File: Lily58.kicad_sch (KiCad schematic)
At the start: 0 parts

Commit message: brainstorming with some components in the schematic
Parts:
- added BAT: Conn_01x02_Pin, Connector_JST:JST_EH_B2B-EH-A_1x02_P2.50mm_Vertical, symbol Connector:Conn_01x02_Pin
- added J1: USB_C_Receptacle, Connector_USB:USB_C_Receptacle_Amphenol_12401548E4-2A_CircularHoles, symbol Connector:USB_C_Receptacle
- added U1: ESP32-S3-WROOM-2, PCM_Espressif:ESP32-S3-WROOM-2, symbol PCM_Espressif:ESP32-S3-WROOM-2
- added U2: D3V3XA4B10LP, Package_DFN_QFN:Diodes_UDFN-10_1.0x2.5mm_P0.5mm, symbol Power_Protection:D3V3XA4B10LP
- added U3: BQ24090DGQ, Package_SO:HVSSOP-10-1EP_3x3mm_P0.5mm_EP1.57x1.88mm_ThermalVias, symbol Battery_Management:BQ24090DGQ
- added U4: AP63203WU, Package_TO_SOT_SMD:TSOT-23-6, symbol Regulator_Switching:AP63203WU
- added Y1: Crystal_GND24, Crystal:Crystal_SMD_3225-4Pin_3.2x2.5mm_HandSoldering, symbol Device:Crystal_GND24
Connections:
- new net: U2.3 (VSS), U2.8 (VSS)
- new net: U3.11 (VSS), U3.3 (VSS)
- new net: J1.A1 (GND), J1.A12 (GND), J1.B1 (GND), J1.B12 (GND)
- new net: J1.A4 (VBUS), J1.A9 (VBUS), J1.B4 (VBUS), J1.B9 (VBUS)
- new net NO: U1.1 (GND), U1.13 (GPIO19/U1RTS/ADC2_CH8/CLK_OUT2/USB_D-), U1.14 (GPIO20/U1CTS/ADC2_CH9/CLK_OUT1/USB_D+), U1.2 (3V3), U1.27 (GPIO0/BOOT), U1.36 (U0RXD/GPIO44/CLK_OUT2), U1.37 (U0TXD/GPIO43/CLK_OUT1), U1.40 (GND), U1.41 (GND)

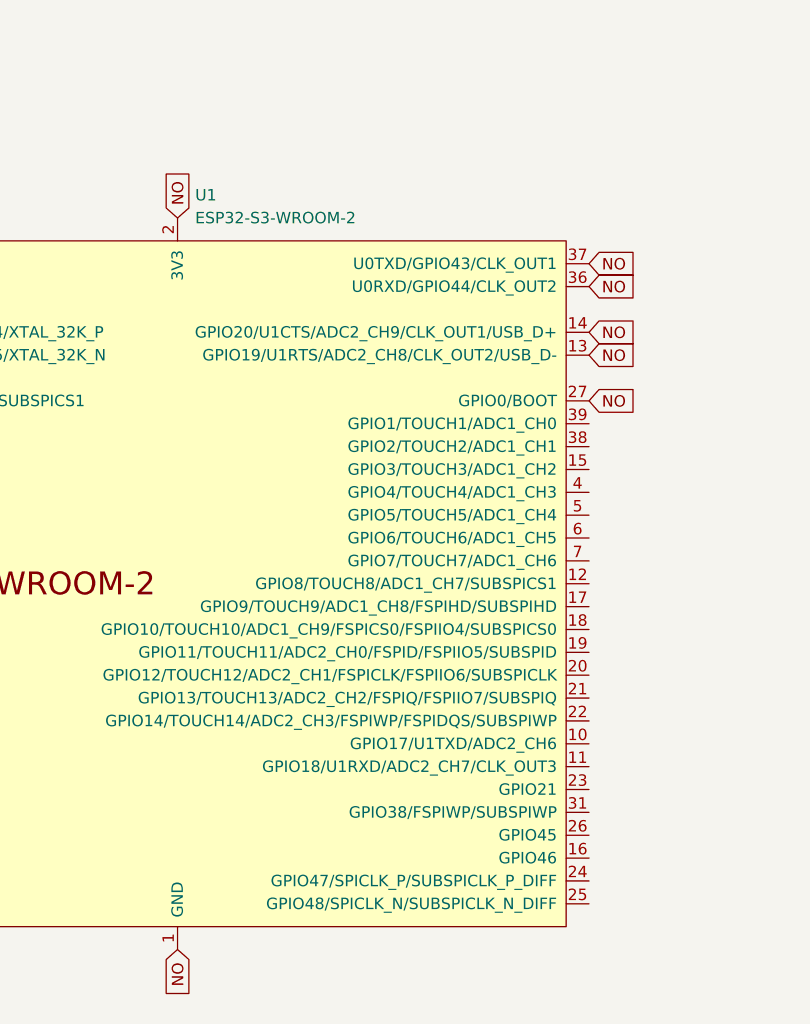
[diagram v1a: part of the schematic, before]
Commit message: added datasheets for MCU, bat-charger & voltage regulator
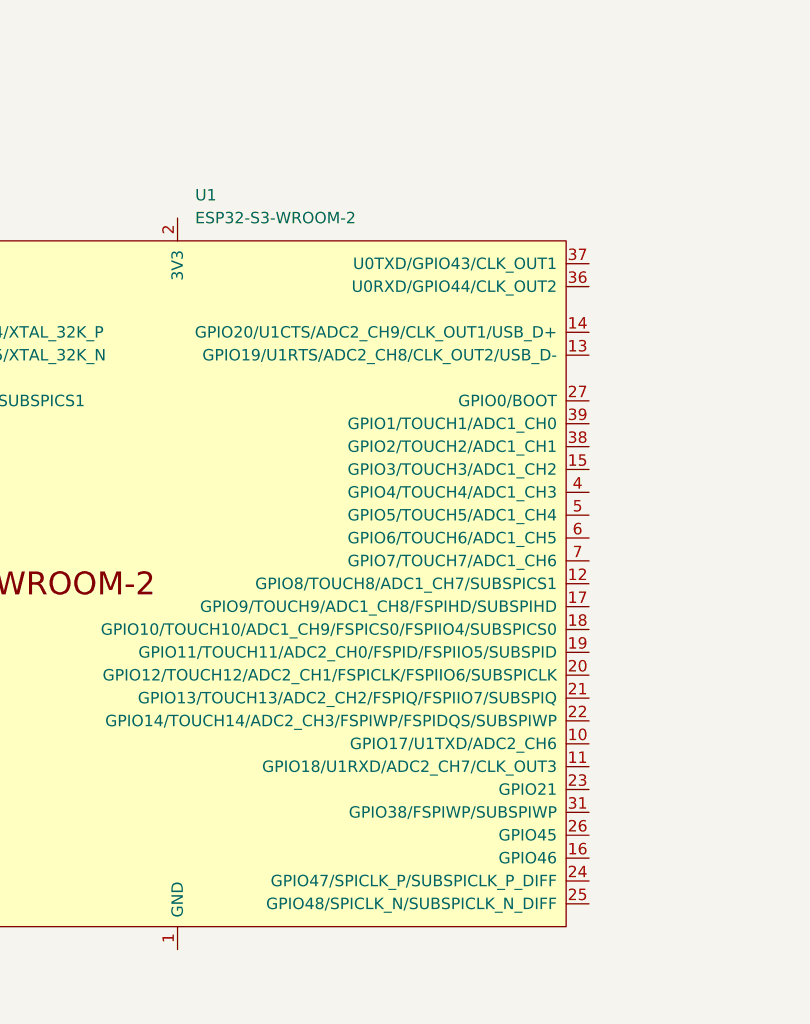
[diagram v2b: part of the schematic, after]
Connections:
- removed net NO: U1.1 (GND), U1.13 (GPIO19/U1RTS/ADC2_CH8/CLK_OUT2/USB_D-), U1.14 (GPIO20/U1CTS/ADC2_CH9/CLK_OUT1/USB_D+), U1.2 (3V3), U1.27 (GPIO0/BOOT), U1.36 (U0RXD/GPIO44/CLK_OUT2), U1.37 (U0TXD/GPIO43/CLK_OUT1), U1.40 (GND), U1.41 (GND)
- new net: U1.1 (GND), U1.40 (GND), U1.41 (GND)
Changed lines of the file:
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@@
 (kicad_sch (version 20230121) (generator eeschema)
   (paper "A4")
-  (global_label "NO" (shape input) (at 138.43 114.3 0) (fields_autoplaced)
-    (effects (font (size 1.27 1.27)) (justify left))
-    (property "Intersheetrefs" "${INTERSHEET_REFS}" (at 143.9968 114.3 0)
-      (effects (font (size 1.27 1.27)) (justify left) hide)
-    )
-  )
-  (global_label "NO" (shape input) (at 138.43 124.46 0) (fields_autoplaced)
-    (effects (font (size 1.27 1.27)) (justify left))
-    (property "Intersheetrefs" "${INTERSHEET_REFS}" (at 143.9968 124.46 0)
-      (effects (font (size 1.27 1.27)) (justify left) hide)
-    )
-  )
-  (global_label "NO" (shape input) (at 138.43 116.84 0) (fields_autoplaced)
-    (effects (font (size 1.27 1.27)) (justify left))
-    (property "Intersheetrefs" "${INTERSHEET_REFS}" (at 143.9968 116.84 0)
-      (effects (font (size 1.27 1.27)) (justify left) hide)
-    )
-  )
-  (global_label "NO" (shape input) (at 92.71 109.22 90) (fields_autoplaced)
-    (effects (font (size 1.27 1.27)) (justify left))
-    (property "Intersheetrefs" "${INTERSHEET_REFS}" (at 92.71 103.6532 90)
-      (effects (font (size 1.27 1.27)) (justify left) hide)
-    )
-  )
-  (global_label "NO" (shape input) (at 138.43 121.92 0) (fields_autoplaced)
-    (effects (font (size 1.27 1.27)) (justify left))
-    (property "Intersheetrefs" "${INTERSHEET_REFS}" (at 143.9968 121.92 0)
-      (effects (font (size 1.27 1.27)) (justify left) hide)
-    )
-  )
-  (global_label "NO" (shape input) (at 92.71 190.5 270) (fields_autoplaced)
-    (effects (font (size 1.27 1.27)) (justify right))
-    (property "Intersheetrefs" "${INTERSHEET_REFS}" (at 92.71 196.0668 90)
-      (effects (font (size 1.27 1.27)) (justify right) hide)
-    )
-  )
-  (global_label "NO" (shape input) (at 138.43 129.54 0) (fields_autoplaced)
-    (effects (font (size 1.27 1.27)) (justify left))
-    (property "Intersheetrefs" "${INTERSHEET_REFS}" (at 143.9968 129.54 0)
-      (effects (font (size 1.27 1.27)) (justify left) hide)
-    )
-  )
   (symbol (lib_id "Connector:Conn_01x02_Pin") (at 208.28 64.77 180) (unit 1)
     (in_bom yes) (on_board yes) (dnp no) (fields_autoplaced)

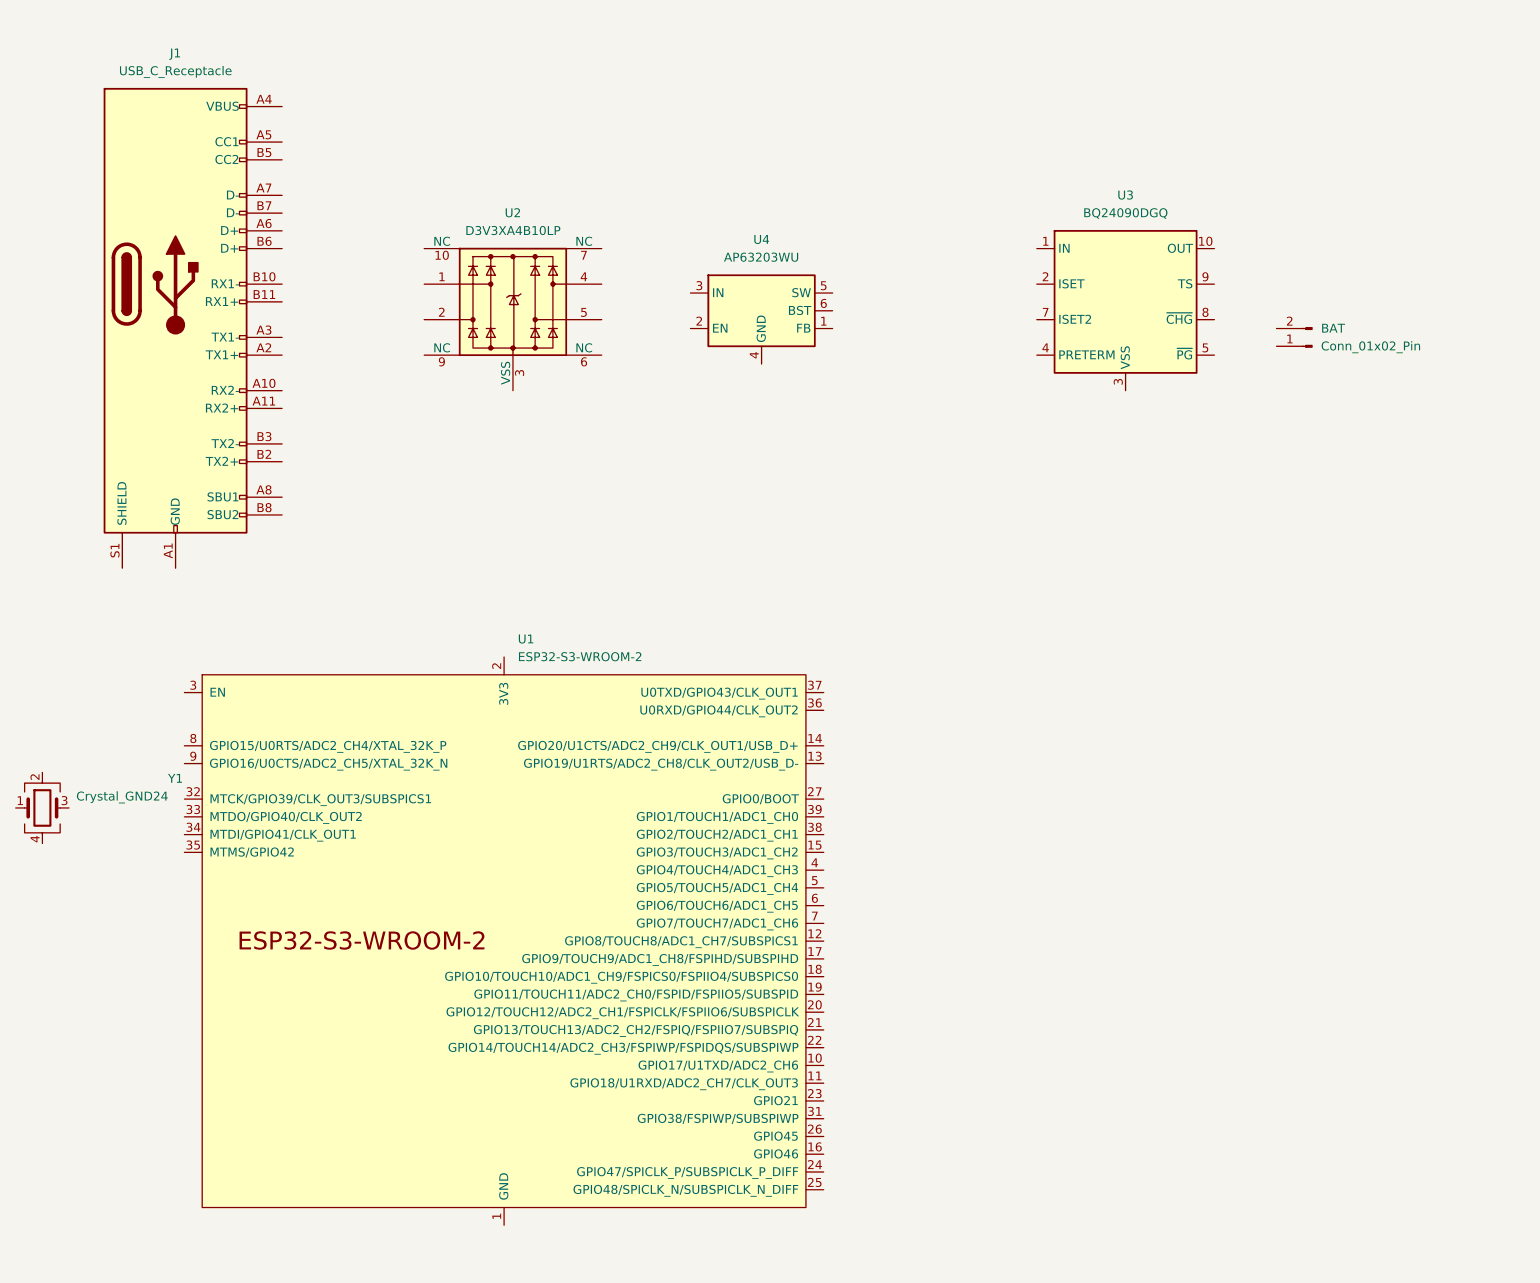
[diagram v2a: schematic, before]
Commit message: AP63203 DC/DC conv. circuit finished
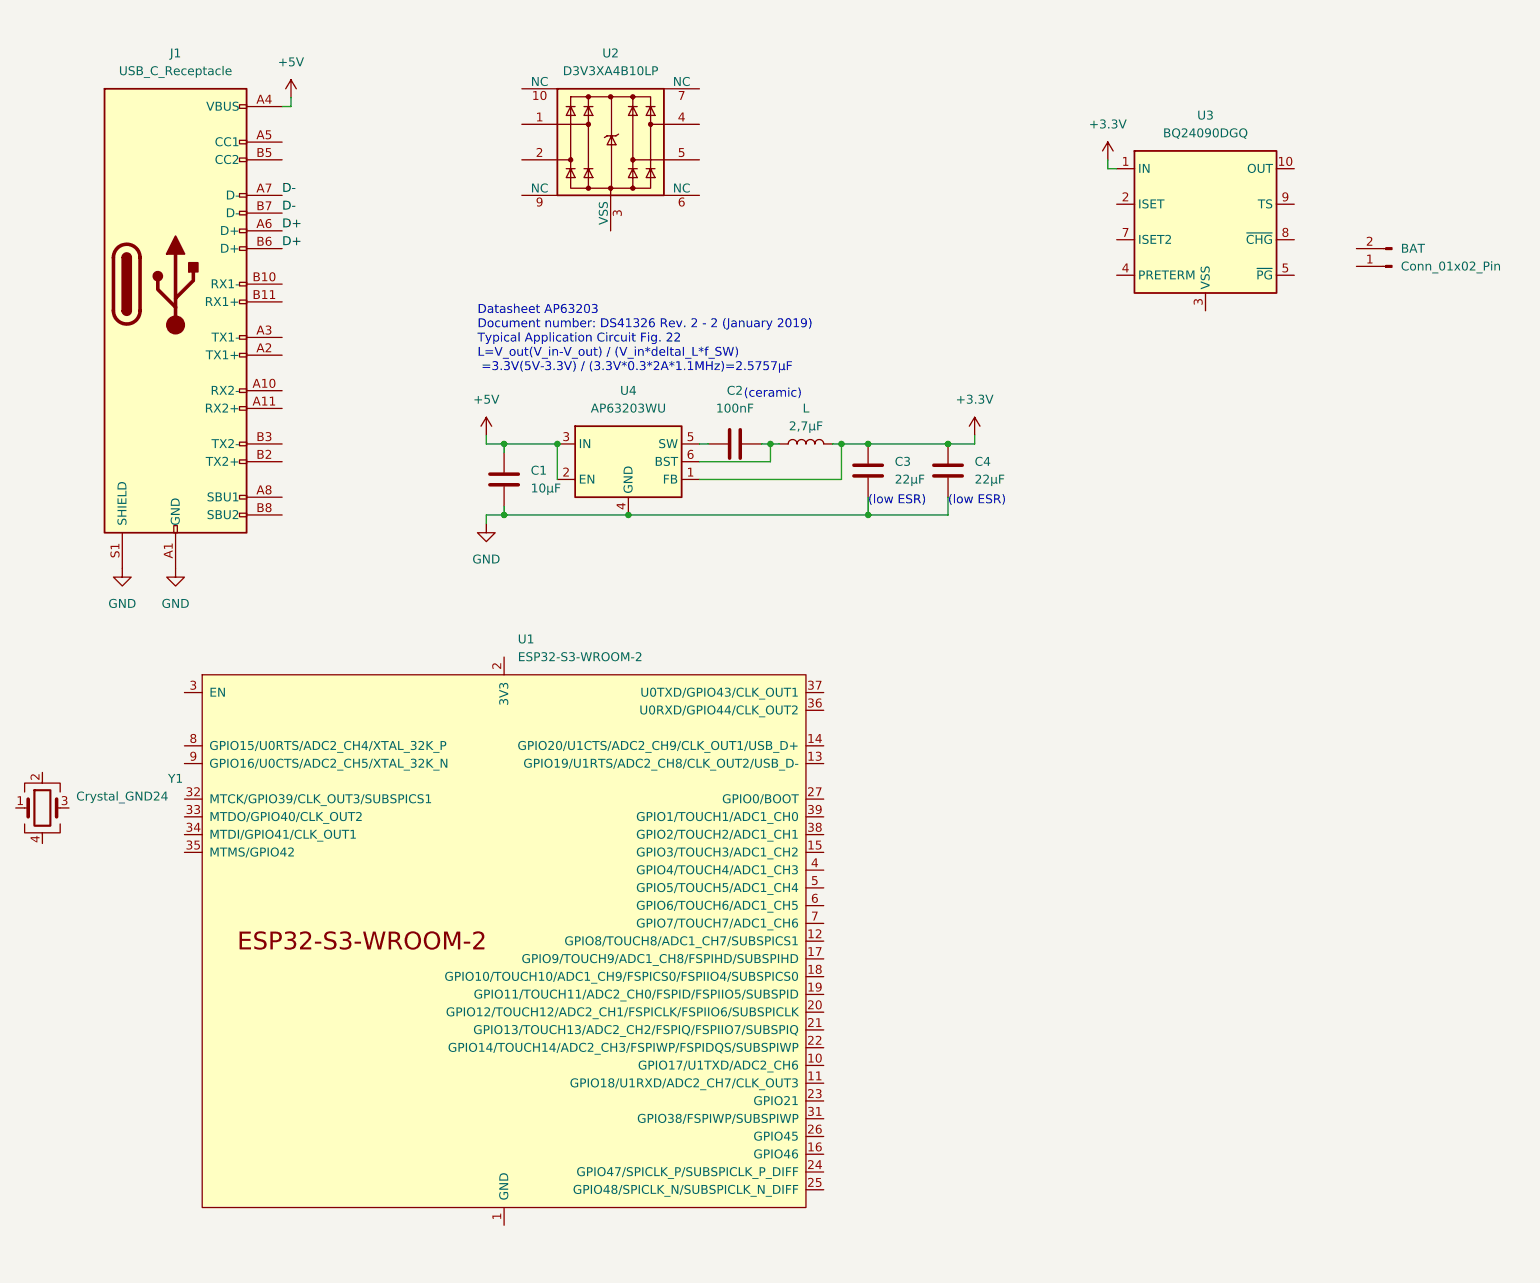
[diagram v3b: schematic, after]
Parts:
- added C1: 10µF, symbol Device:C
- added C2: 100nF, symbol Device:C
- added C3, C4: 22µF, symbol Device:C
- added L: 2,7µF, symbol Device:L
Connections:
- net +3.3V: now reaches U4.1 (FB)
- net +3.3V: now also U3.1 (IN), C3.1, C4.1, L.2
- net +5V: now reaches U4.2 (EN)
- net +5V: now also J1.A4 (VBUS), J1.A9 (VBUS), J1.B4 (VBUS), J1.B9 (VBUS), U4.3 (IN), C1.1
- net GND: now reaches U4.4 (GND)
- net GND: now also J1.A1 (GND), J1.A12 (GND), J1.B1 (GND), J1.B12 (GND), J1.S1 (SHIELD), C1.2, C3.2, C4.2
- net at U4.5 (SW): now also C2.1
- net at U4.6 (BST): now also C2.2, L.1
- net D+: now reaches J1.A6 (D+)
- net D+: now also J1.B6 (D+)
- net D-: now reaches J1.A7 (D-)
- net D-: now also J1.B7 (D-)
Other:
- note added: "(ceramic)"
- note added: "(low ESR)"
- note added: "Datasheet AP63203 Document number: DS41326 Rev. 2 - 2 (January 2019) Typical Application Circuit Fig. 22 L=V_out(V_in-V_out) / (V_in*deltaI_L*f_SW) =3.3V(5V-3.3V) / (3.3V*0.3*2A*1.1MHz)=2.5757µF"
- moved on the sheet: BAT, U2, U3, U4

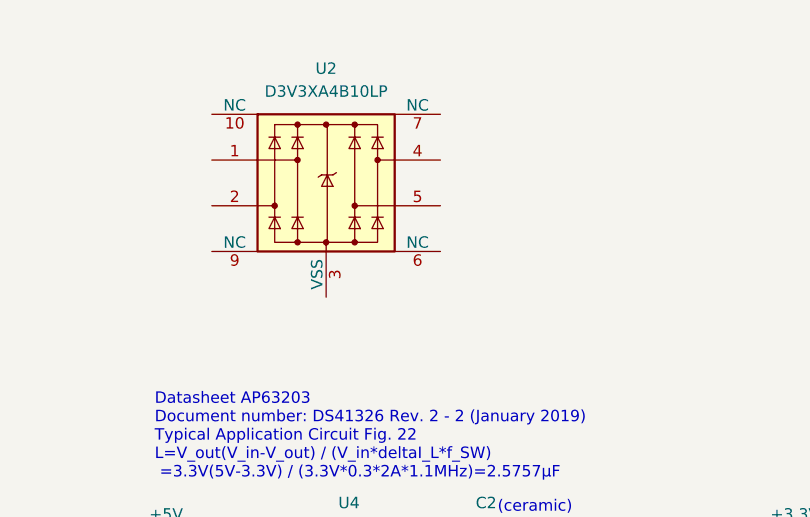
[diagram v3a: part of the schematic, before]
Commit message: TVS Diode array connected
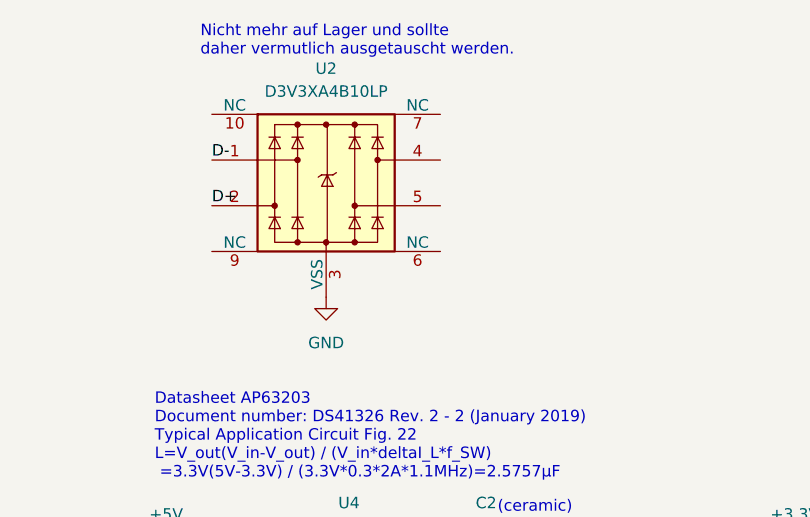
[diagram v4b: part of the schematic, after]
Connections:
- net D+: now also U2.2
- net D-: now also U2.1
- net GND: now also U2.3 (VSS), U2.8 (VSS)
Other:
- note added: "Nicht mehr auf Lager und sollte daher vermutlich ausgetauscht werden."
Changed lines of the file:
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@@
+    (effects (font (size 1.27 1.27)) (justify left bottom))
+  )
+  (text "Nicht mehr auf Lager und sollte\ndaher vermutlich ausgetauscht werden.\n"
+    (at 93.98 21.59 0)
     (effects (font (size 1.27 1.27)) (justify left bottom))
   )
@@
     (effects (font (size 1.27 1.27)) (justify left bottom))
   )
+  (label "D-" (at 95.25 33.02 0) (fields_autoplaced)
+    (effects (font (size 1.27 1.27)) (justify left bottom))
+  )
   (label "D-" (at 60.96 45.72 0) (fields_autoplaced)
     (effects (font (size 1.27 1.27)) (justify left bottom))
   )
   (label "D-" (at 60.96 43.18 0) (fields_autoplaced)
+    (effects (font (size 1.27 1.27)) (justify left bottom))
+  )
+  (label "D+" (at 95.25 38.1 0) (fields_autoplaced)
     (effects (font (size 1.27 1.27)) (justify left bottom))
   )
@@
         )
       )
+    )
+  )
+  (symbol (lib_id "power:GND") (at 107.95 48.26 0) (unit 1)
+    (in_bom yes) (on_board yes) (dnp no) (fields_autoplaced)
+    (property "Reference" "#PWR08" (at 107.95 54.61 0)
+      (effects (font (size 1.27 1.27)) hide)
+    )
+    (property "Value" "GND" (at 107.95 53.34 0)
+      (effects (font (size 1.27 1.27)))
+    )
+    (property "Footprint" "" (at 107.95 48.26 0)
+      (effects (font (size 1.27 1.27)) hide)
+    )
+    (property "Datasheet" "" (at 107.95 48.26 0)
+      (effects (font (size 1.27 1.27)) hide)
+    )
+    (pin "1")
+    (instances
+      (project "Lily58"
+        (path "/a0958e12-2248-4ac3-b259-3086ac296b70"
+          (reference "#PWR08") (unit 1)
+        )
+      )

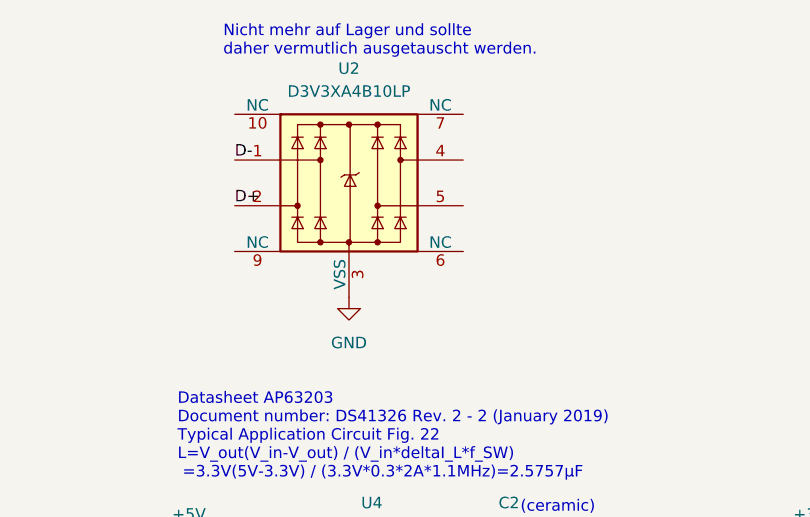
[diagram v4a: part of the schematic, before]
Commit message: swapped TVS diode array for ESD7104 diode array; added symbol and datasheet
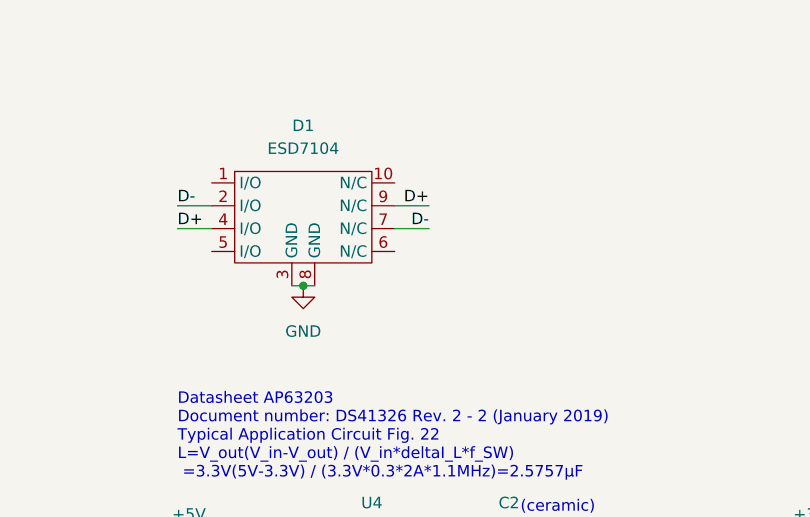
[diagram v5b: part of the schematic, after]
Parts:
- removed U2: D3V3XA4B10LP, Package_DFN_QFN:Diodes_UDFN-10_1.0x2.5mm_P0.5mm, symbol Power_Protection:D3V3XA4B10LP
- added D1: ESD7104, symbol Lily58:ESD7104
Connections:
- net D+: now also D1.4 (I/O), D1.9 (N/C)
- net D-: now also D1.2 (I/O), D1.7 (N/C)
- net GND: now also D1.3 (GND), D1.8 (GND)
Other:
- note removed: "Nicht mehr auf Lager und sollte daher vermutlich ausgetauscht werden."

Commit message: ESD7104 UDFN-10 footprints added and datasheet linked
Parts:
- D1: footprint (none) -> Lily58:UDFN10 2.5x1 0.5Pitch wide center pad
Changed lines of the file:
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@@
       (effects (font (size 1.27 1.27)))
     )
-    (property "Footprint" "" (at 101.6 38.1 0)
+    (property "Footprint" "Lily58:UDFN10 2.5x1 0.5Pitch wide center pad" (at 102.87 57.15 0)
       (effects (font (size 1.27 1.27)) hide)
     )
-    (property "Datasheet" "" (at 101.6 38.1 0)
+    (property "Datasheet" "${KIPROJMOD}/datasheets/ESD7104-D.pdf" (at 102.87 54.61 0)
       (effects (font (size 1.27 1.27)) hide)
     )
     (pin "9")
-    (pin "6")
+    (pin "8")
+    (pin "4")
     (pin "2")
-    (pin "8")
-    (pin "7")
-    (pin "5")
     (pin "3")
     (pin "10")
     (pin "1")
-    (pin "4")
+    (pin "5")
+    (pin "6")
+    (pin "7")
     (instances
       (project "Lily58"
